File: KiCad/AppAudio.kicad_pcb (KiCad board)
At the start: 2 copper layers, 60 x 62 mm, 34 parts, among them P1 WRITER-VCC, Q1 Q_NMOS_SGD, SW1 SW_PUSH, SW2 SW_PUSH, U1 TWE_LITE_SMD, U2 LMC6062, U3 HT82V739

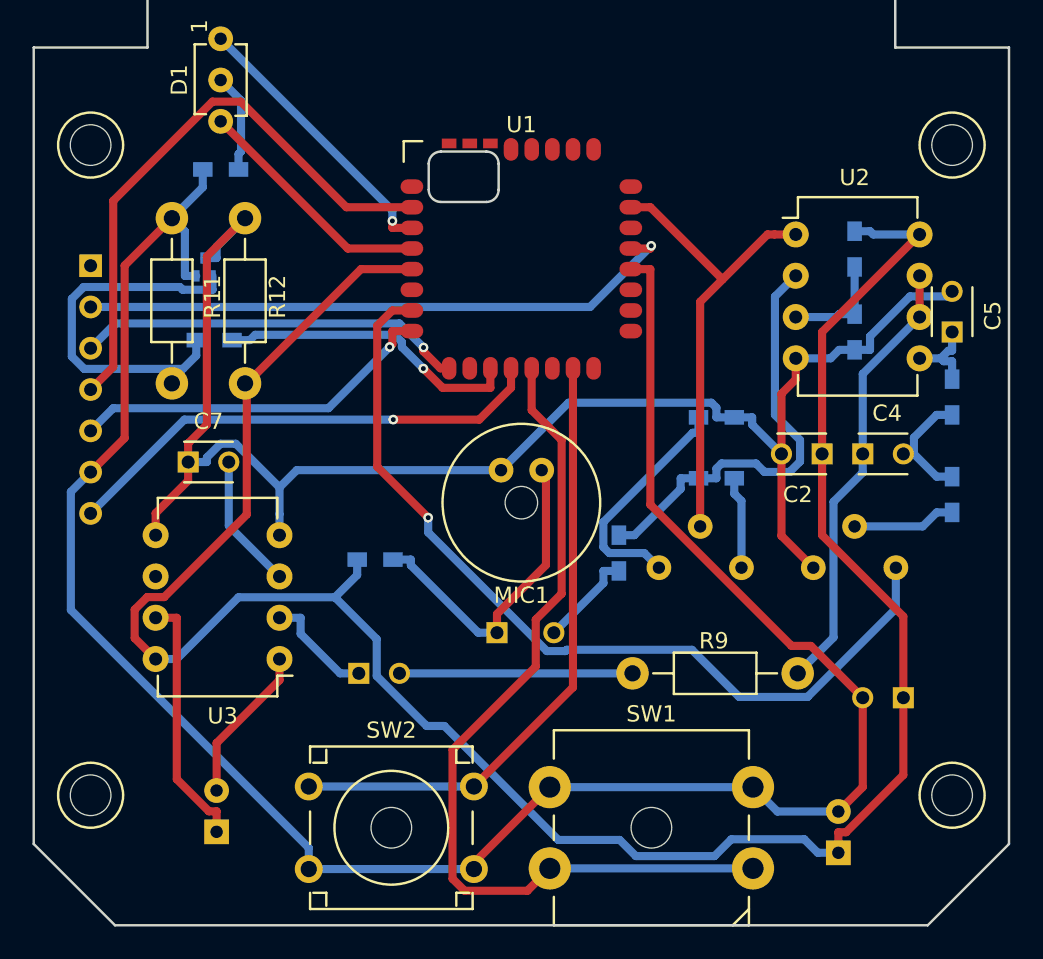
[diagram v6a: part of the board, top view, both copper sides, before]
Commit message: Replaced the footprint of SW2.
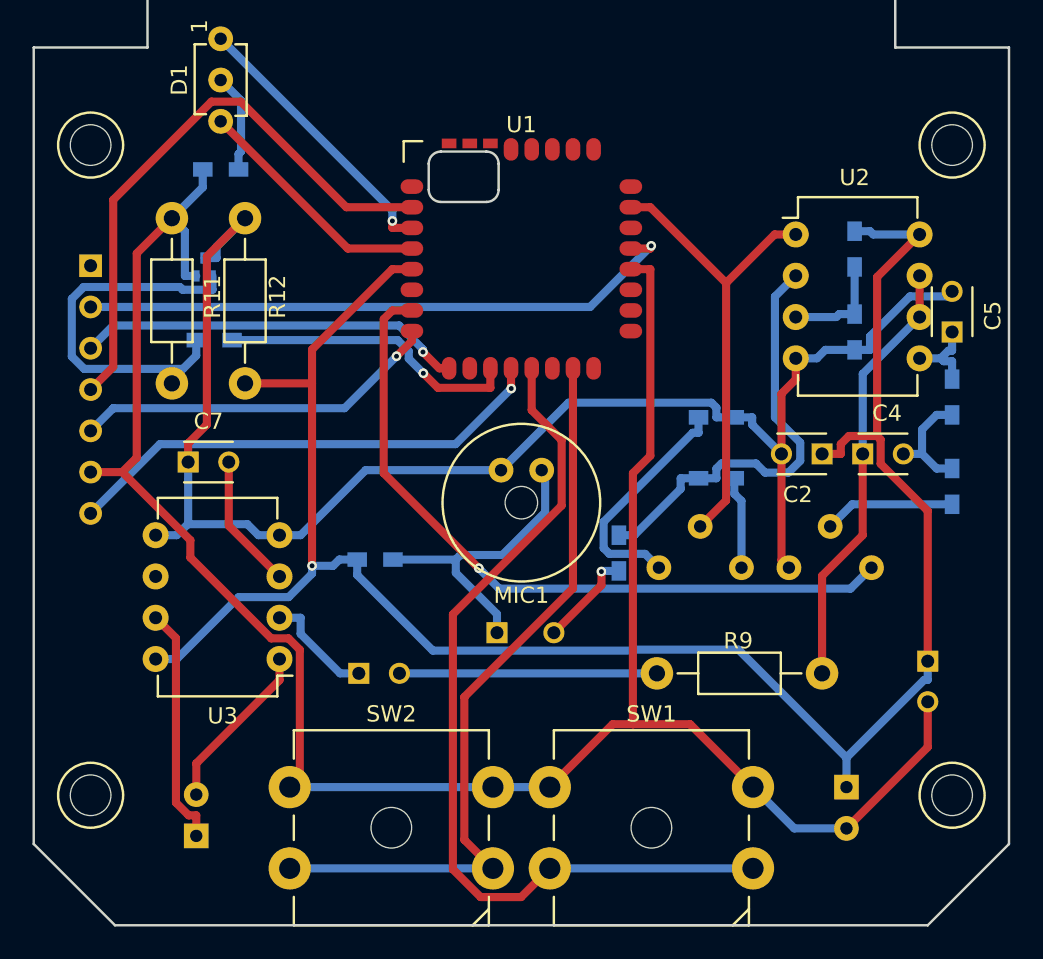
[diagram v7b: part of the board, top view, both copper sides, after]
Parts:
- SW2: footprint favorites:JB-15HFBP2 -> favorites:TVGP01-G73BB
- moved BT1 4.07 mm to (120.0, 119.5), turned to 180 degrees
- moved C3 2.70 mm to (125.0, 111.8), turned to 270 degrees
- moved R9 1.50 mm to (108.3, 112.5)
- moved VR2 1.50 mm to (119.0, 106.0)
- moved SP1 1.27 mm to (80.0, 122.5)
- moved R7 0.50 mm to (126.5, 101.0)
- turned SW2 to 180 degrees
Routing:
- net VCC: track 137.9 -> 123.4 mm, vias 0 -> 1
- net Net-(U1-Pad7): track 54.3 -> 44.9 mm
- net Net-(SW2-Pad1): track 38.4 -> 46.8 mm
- net GND: track 133.8 -> 130.0 mm
- net VSS: track 96.8 -> 93.8 mm
- net Net-(R7-Pad2): track 6.36 -> 8.06 mm
- net Net-(C6-Pad2): track 14.3 -> 15.8 mm
- net /OUTP: track 15.8 -> 14.7 mm
- net Net-(C1-Pad1): track 19.8 -> 18.8 mm
- net /OUTN: track 9.69 -> 10.5 mm
- net Net-(C4-Pad1): track 27.6 -> 26.9 mm
- net Net-(C1-Pad2): track 6.01 -> 6.06 mm, vias 0 -> 1

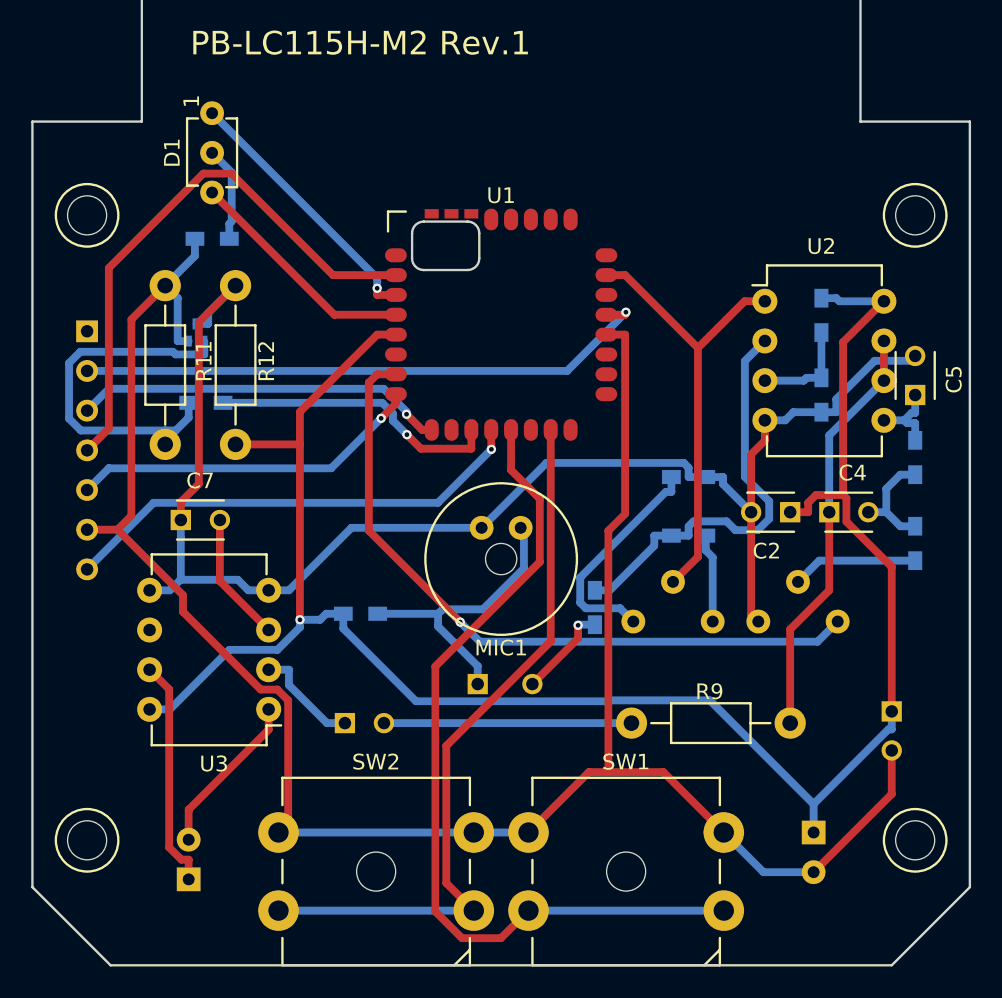
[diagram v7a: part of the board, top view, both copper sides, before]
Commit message: Removed the net file.
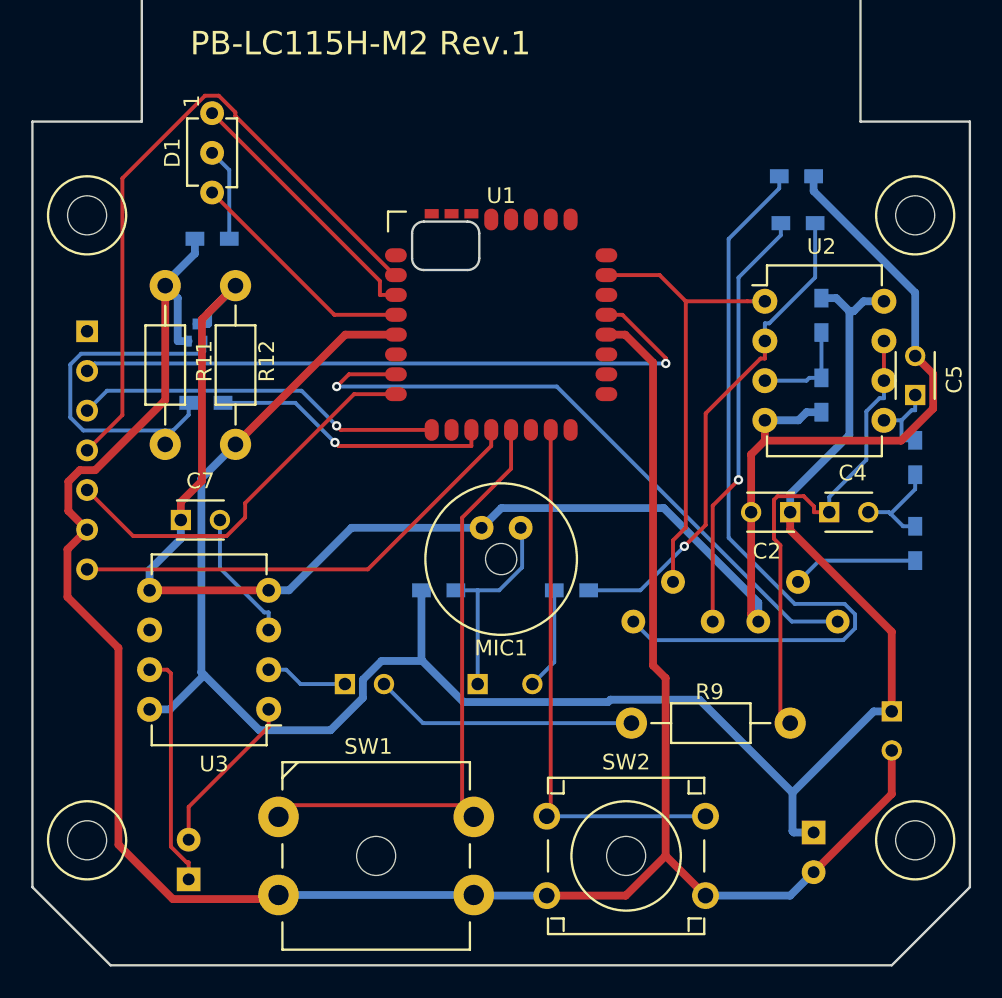
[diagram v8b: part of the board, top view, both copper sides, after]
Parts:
- SW2: footprint favorites:TVGP01-G73BB -> favorites:JB-15HFBP2
- moved R5 21.2 mm to (119.0, 80.5), turned to 0 degrees
- moved R6 20.4 mm to (118.9, 77.5)
- moved SW1 16.0 mm to (92.0, 121.0), turned to 0 degrees
- moved SW2 16.0 mm to (108.0, 121.0), turned to 90 degrees
- moved R1 5.22 mm to (96.0, 104.0)
- moved C6 2.50 mm to (90.0, 110.0)
- moved R2 1.86 mm to (104.5, 104.0), turned to 180 degrees
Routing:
- net Net-(R6-Pad2): track 14.6 -> 50.5 mm
- net VSS: track 93.8 -> 117.5 mm
- net Net-(R5-Pad1): track 5.68 -> 27.3 mm, vias 0 -> 1
- net Net-(SW1-Pad1): track 54.3 -> 38.4 mm
- net GND: track 130.0 -> 144.0 mm
- net Net-(SW2-Pad1): track 46.8 -> 35.0 mm
- net /PRG: track 35.8 -> 42.9 mm
- net VCC: track 123.4 -> 130.0 mm, vias 1 -> 0
- net Net-(C1-Pad1): track 18.8 -> 13.4 mm
- net /RST: track 37.4 -> 42.5 mm
- net Net-(R2-Pad1): track 26.8 -> 31.8 mm, vias 0 -> 1
- net Net-(C4-Pad1): track 26.9 -> 31.6 mm
- net /TXD: track 22.7 -> 25.3 mm, vias 1 -> 0
- net Net-(U1-Pad7): track 44.9 -> 42.4 mm
- net /Aud_In: track 6.88 -> 5.26 mm
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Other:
- net class Default: trace_width 0.5 -> 0.25
- net class Power added: clearance 0.25, trace_width 0.5, via_dia 0.6, via_drill 0.4
